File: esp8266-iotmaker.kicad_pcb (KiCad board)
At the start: 2 copper layers, 47.2 x 25.7 mm, 54 parts, among them J1 CONN_01X10, J2 CONN_01X10, Q1 S8050, Q2 S8050, SW1 SW_Push, SW2 SW_Push, U1 usb_mini_b, U2 chip-esp8266, U3 CP2102, U4 25Q32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

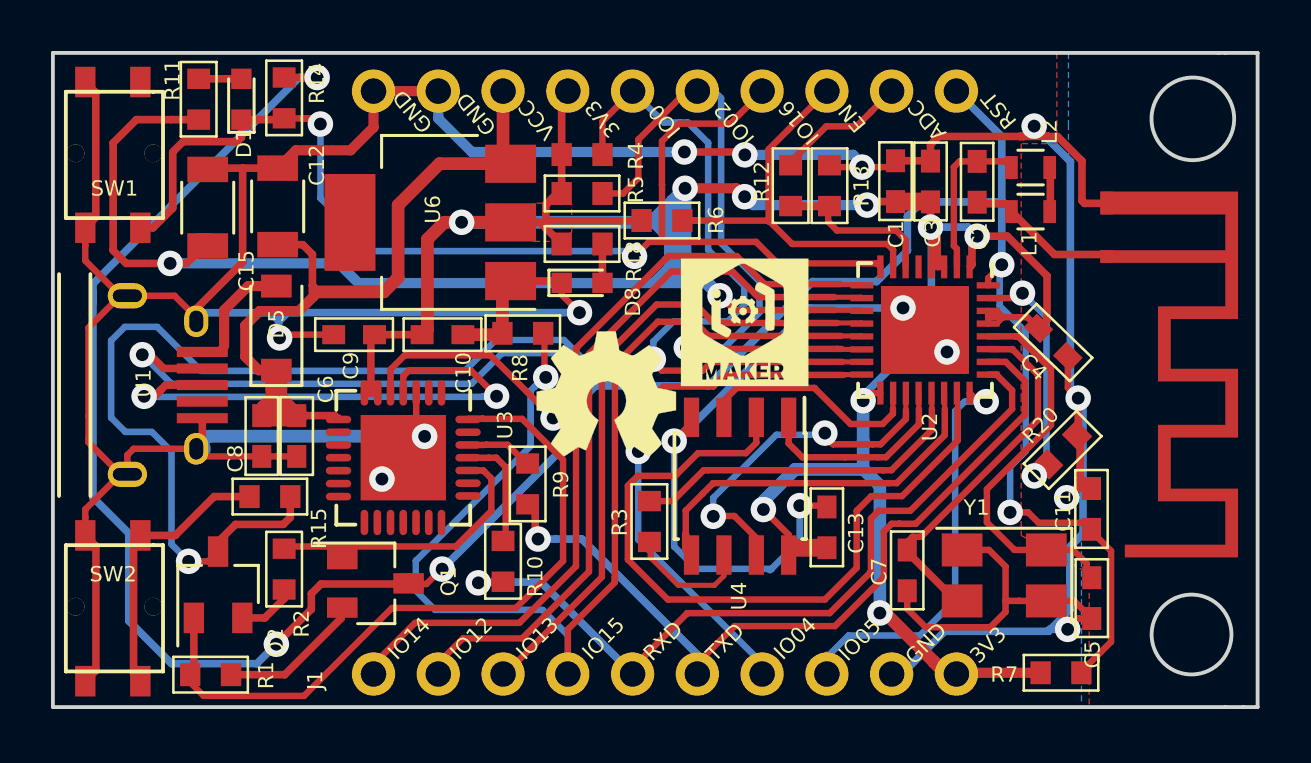
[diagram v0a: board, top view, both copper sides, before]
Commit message: change footprint usb
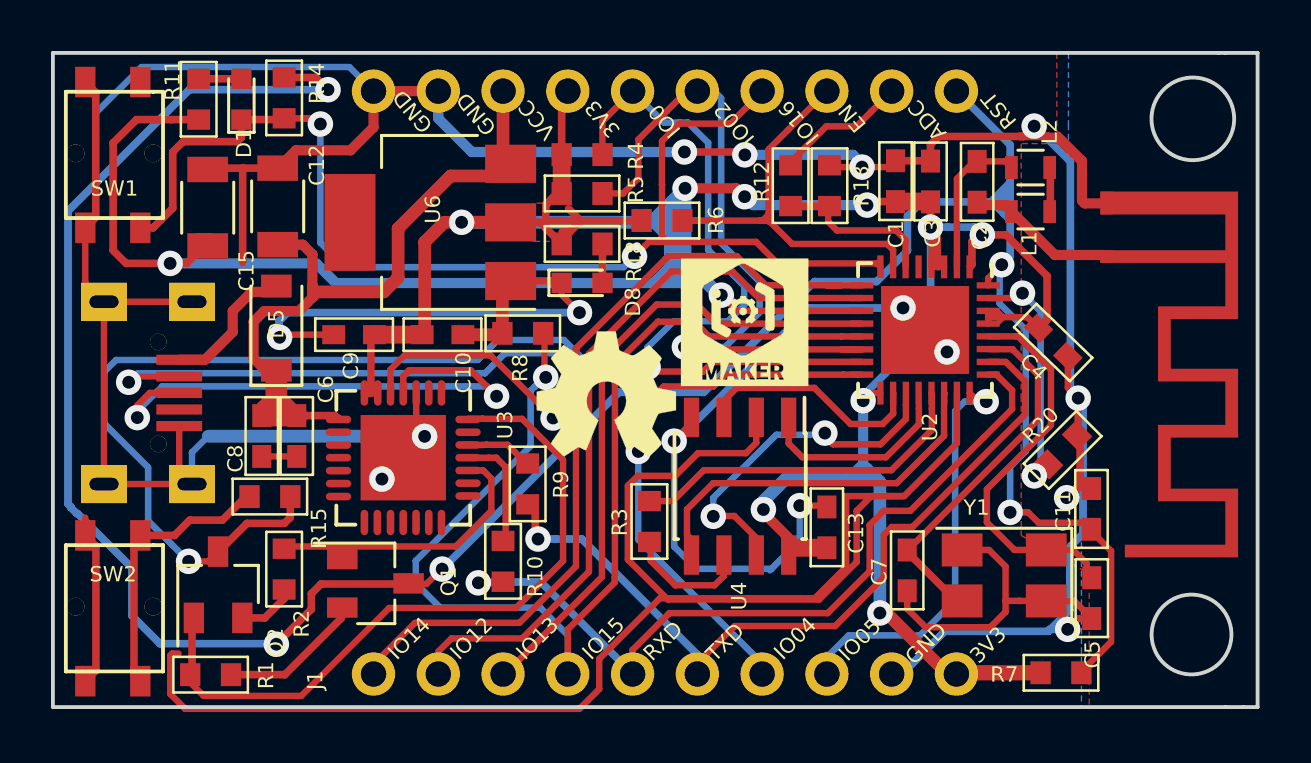
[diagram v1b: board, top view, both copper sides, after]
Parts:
- moved U1 3.86 mm to (131.5, 98.6)
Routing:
- net MOSI: track 29.0 -> 65.5 mm
- net REST: track 101.2 -> 107.9 mm
- net 3V3: track 150.2 -> 153.9 mm
- net GPIO0: track 66.9 -> 64.6 mm
- net GPIO16: track 46.6 -> 48.3 mm
- net GND: track 219.0 -> 220.6 mm
- net Net-(AE1-Pad1): track 6.03 -> 6.92 mm
- net GPIO12: track 28.8 -> 29.6 mm
- net D-: track 31.6 -> 30.9 mm
- net VUSB: track 4.80 -> 5.49 mm
- net D+: track 21.4 -> 22.1 mm
- net GPIO14: track 33.0 -> 33.5 mm
